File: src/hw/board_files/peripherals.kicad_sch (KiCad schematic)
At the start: 35 parts, among them J3 Screw_Terminal_01x03, J4 Molex 104031-0811, Q1 PMOS, U4 NEO-M9N, U5 BQ27411DRZT-G1A, U6 SHT30-DIS

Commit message: Layout progress
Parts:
- removed JP1, JP2: Solder_Jumper, Jumper:SolderJumper-2_P1.3mm_Open_TrianglePad1.0x1.5mm, symbol Jumper:Jumper_2_Small_Bridged
- TP8, TP9: footprint TestPoint:TestPoint_Pad_D1.5mm -> TestPoint:TestPoint_Pad_D1.0mm
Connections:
- net +3V3: now also U4.1 (~{SAFEBOOT}), U4.2 (D_SEL)
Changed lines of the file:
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@@
 	(wire
 		(pts
-			(xy 40.64 86.36) (xy 53.34 86.36)
+			(xy 40.64 86.36) (xy 63.5 86.36)
 		)
 		(stroke
@@
 	(wire
 		(pts
-			(xy 58.42 86.36) (xy 63.5 86.36)
-		)
-		(stroke
-			(width 0)
-			(type default)
-		)
-	)
-	(wire
-		(pts
-			(xy 58.42 91.44) (xy 63.5 91.44)
-		)
-		(stroke
-			(width 0)
-			(type default)
-		)
-	)
-	(wire
-		(pts
 			(xy 27.94 138.43) (xy 26.67 138.43)
 		)
@@
 	(wire
 		(pts
-			(xy 40.64 91.44) (xy 53.34 91.44)
+			(xy 40.64 91.44) (xy 63.5 91.44)
 		)
 		(stroke
@@
 			)
 		)
-		(property "Footprint" "TestPoint:TestPoint_Pad_D1.5mm"
+		(property "Footprint" "TestPoint:TestPoint_Pad_D1.0mm"
 			(at 137.16 147.32 0)
 			(effects
@@
 	)
 	(symbol
-		(lib_id "Jumper:Jumper_2_Small_Bridged")
-		(at 55.88 91.44 0)
-		(unit 1)
-		(exclude_from_sim no)
-		(in_bom yes)
-		(on_board yes)
-		(dnp no)
-		(fields_autoplaced yes)
-		(property "Reference" "JP2"
-			(at 55.88 93.98 0)
-			(effects
-				(font
-					(size 1.27 1.27)
-				)
-			)
-		)
-		(property "Value" "Solder_Jumper"
-			(at 55.88 96.52 0)
-			(effects
-				(font
-					(size 1.27 1.27)
-				)
-			)
-		)
-		(property "Footprint" "Jumper:SolderJumper-2_P1.3mm_Open_TrianglePad1.0x1.5mm"
-			(at 55.88 91.44 0)
-			(effects
-				(font
-					(size 1.27 1.27)
-				)
-				(hide yes)
-			)
-		)
-		(property "Datasheet" "~"
-			(at 55.88 91.44 0)
-			(effects
-				(font
-					(size 1.27 1.27)
-				)
-				(hide yes)
-			)
-		)
-		(property "Description" "Jumper, 2-pole, small symbol, bridged"
-			(at 55.88 91.44 0)
-			(effects
-				(font
-					(size 1.27 1.27)
-				)
-				(hide yes)
-			)
-		)
-		(pin "1"
-		)
-		(pin "2"
-		)
-		(instances
-			(project ""
-				(path "/2c77a8ba-b277-4959-adec-d3fc778c7960/81382524-b053-4c3c-9e13-c8b314c52639"
-					(reference "JP2")
-					(unit 1)
-				)
-			)
-		)
-	)
-	(symbol
 		(lib_id "Device:R_Small_US")
 		(at 144.78 147.32 270)
@@
 		(on_board yes)
 		(dnp no)
-		(fields_autoplaced yes)
 		(property "Reference" "C22"
 			(at 158.75 151.1235 0)
@@
 					(size 1.27 1.27)
 				)
-				(justify right)
+				(justify left)
 			)
 		)
@@
 	)
 	(symbol
-		(lib_id "Jumper:Jumper_2_Small_Bridged")
-		(at 55.88 86.36 0)
-		(unit 1)
-		(exclude_from_sim no)
-		(in_bom yes)
-		(on_board yes)
-		(dnp no)
-		(property "Reference" "JP1"
-			(at 55.88 81.28 0)
-			(effects
-				(font
-					(size 1.27 1.27)
-				)
-			)
-		)
-		(property "Value" "Solder_Jumper"
-			(at 55.88 83.82 0)
-			(effects
-				(font
-					(size 1.27 1.27)
-				)
-			)
-		)
-		(property "Footprint" "Jumper:SolderJumper-2_P1.3mm_Open_TrianglePad1.0x1.5mm"
-			(at 55.88 86.36 0)
-			(effects
-				(font
-					(size 1.27 1.27)
-				)
-				(hide yes)
-			)
-		)
-		(property "Datasheet" "~"
-			(at 55.88 86.36 0)
-			(effects
-				(font
-					(size 1.27 1.27)
-				)
-				(hide yes)
-			)
-		)
-		(property "Description" "Jumper, 2-pole, small symbol, bridged"
-			(at 55.88 86.36 0)
-			(effects
-				(font
-					(size 1.27 1.27)
-				)
-				(hide yes)
-			)
-		)
-		(pin "1"
-		)
-		(pin "2"
-		)
-		(instances
-			(project "pocket-caddy"
-				(path "/2c77a8ba-b277-4959-adec-d3fc778c7960/81382524-b053-4c3c-9e13-c8b314c52639"
-					(reference "JP1")
-					(unit 1)
-				)
-			)
-		)
-	)
-	(symbol
 		(lib_id "Device:R_Small_US")
 		(at 134.62 152.4 180)
@@
 			)
 		)
-		(property "Footprint" "TestPoint:TestPoint_Pad_D1.5mm"
+		(property "Footprint" "TestPoint:TestPoint_Pad_D1.0mm"
 			(at 250.19 44.45 0)
 			(effects

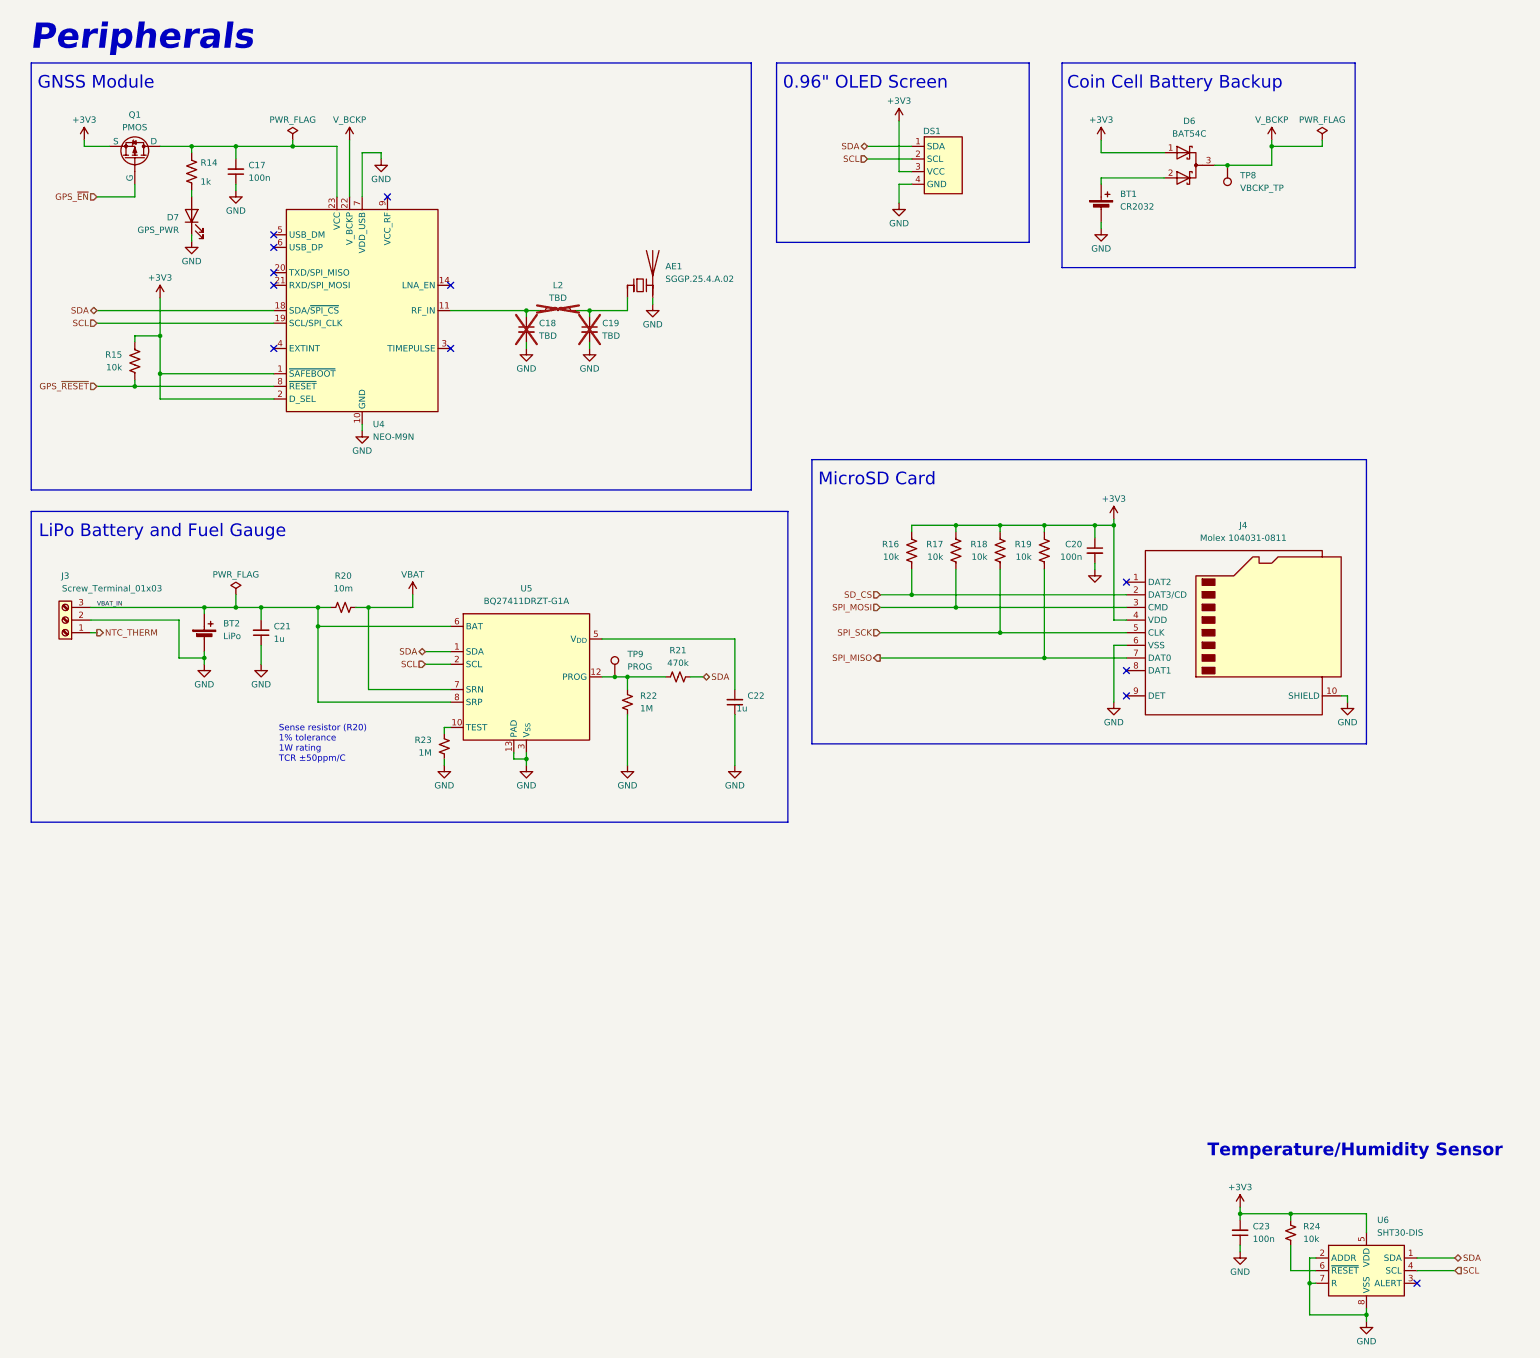
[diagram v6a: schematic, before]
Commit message: New layout done, need to make gerbers
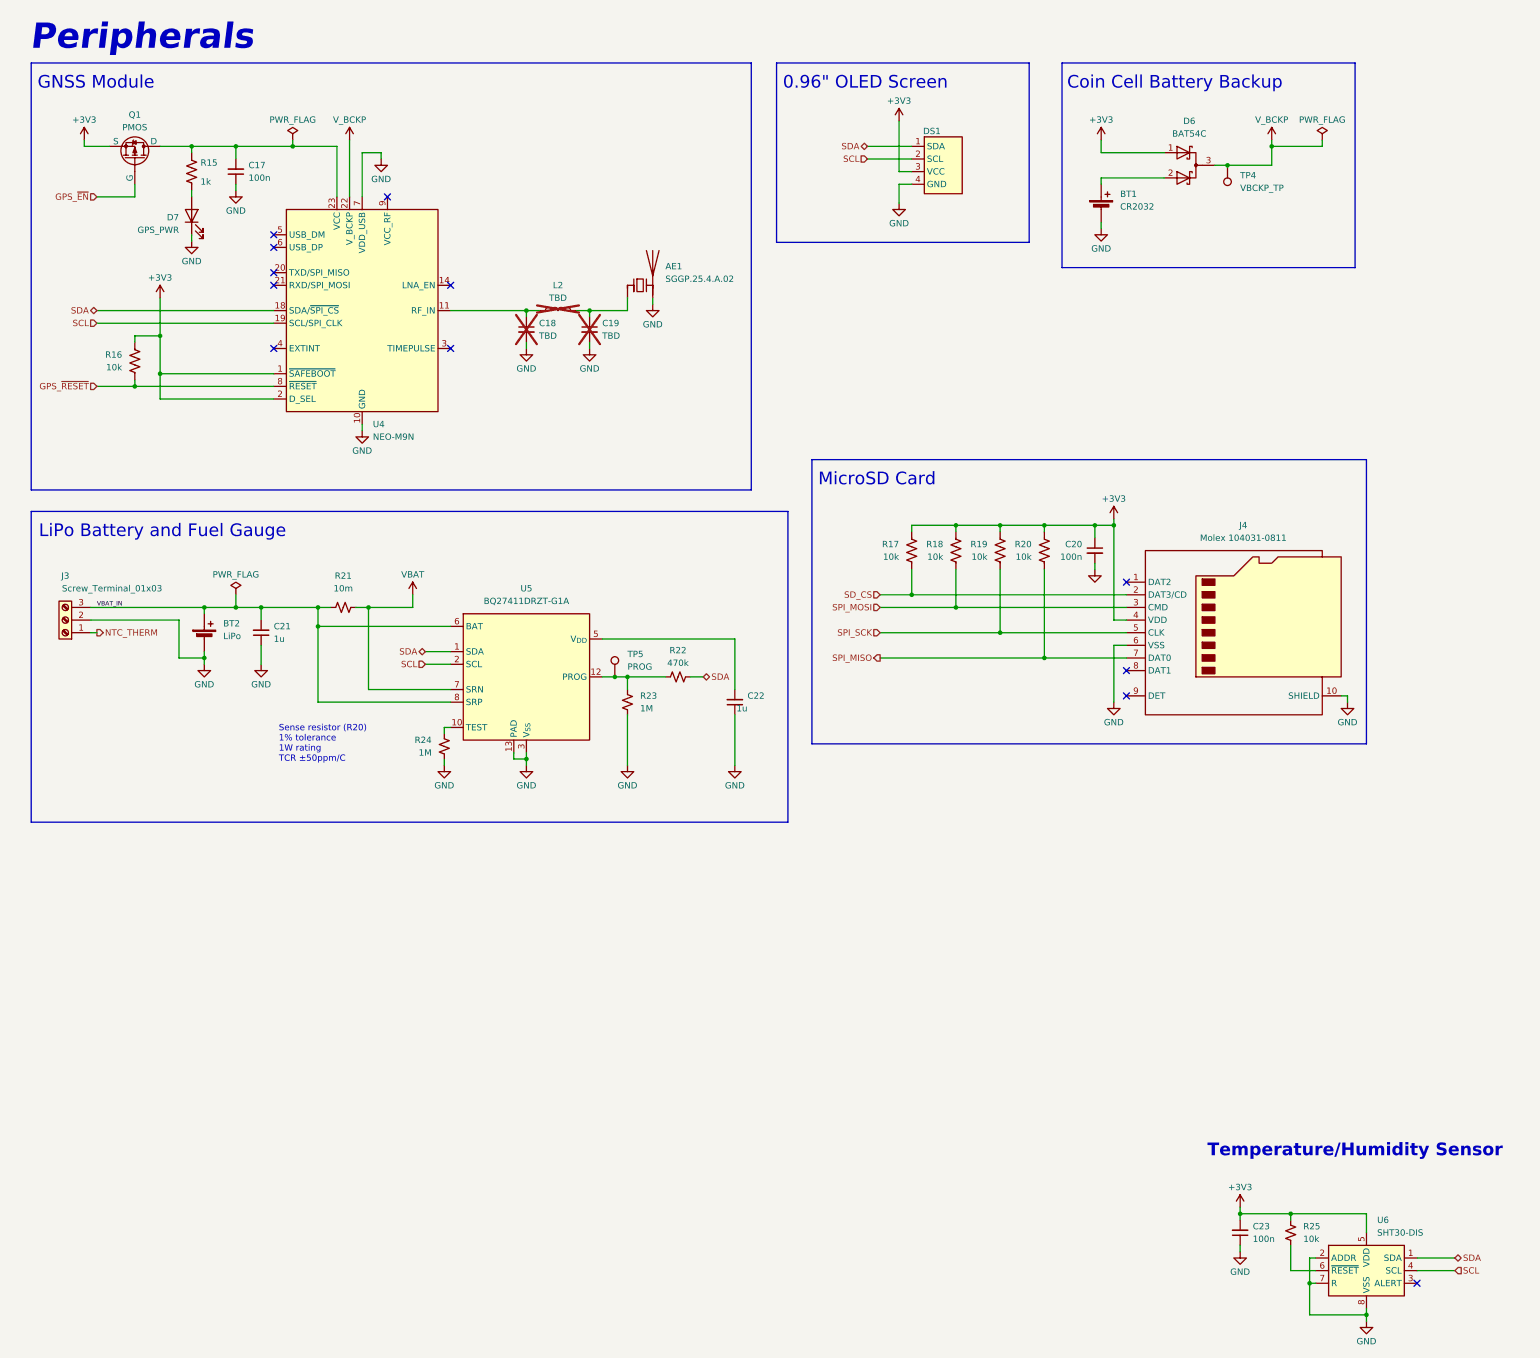
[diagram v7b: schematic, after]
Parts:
- renumbered R14 to R15, R15 to R16, R16 to R17, R17 to R18, R18 to R19, R19 to R20, R20 to R21, R21 to R22, R22 to R23, R23 to R24, R24 to R25, TP8 to TP4, TP9 to TP5

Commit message: rev0.1 done
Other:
- note added: "Sense resistor (R21) 1% tolerance 1W rating TCR ±50ppm/C"
- note removed: "Sense resistor (R20) 1% tolerance 1W rating TCR ±50ppm/C"
- moved on the sheet: C23, R25, U6
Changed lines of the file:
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@@
 		)
 	)
-	(text "Sense resistor (R20)\n1% tolerance\n1W rating\nTCR ±50ppm/C"
+	(text "Sense resistor (R21)\n1% tolerance\n1W rating\nTCR ±50ppm/C"
 		(exclude_from_sim no)
 		(at 64.516 160.782 0)
@@
 	(text "Temperature/Humidity Sensor"
 		(exclude_from_sim no)
-		(at 280.924 242.57 0)
+		(at 193.294 63.5 0)
 		(effects
 			(font
@@
 	)
 	(junction
-		(at 283.21 275.59)
+		(at 195.58 96.52)
 		(diameter 0)
 		(color 0 0 0 0)
@@
 	)
 	(junction
-		(at 271.78 269.24)
+		(at 184.15 90.17)
 		(diameter 0)
 		(color 0 0 0 0)
@@
 	)
 	(junction
-		(at 257.81 255.27)
+		(at 170.18 76.2)
 		(diameter 0)
 		(color 0 0 0 0)
@@
 	)
 	(junction
-		(at 267.97 255.27)
+		(at 180.34 76.2)
 		(diameter 0)
 		(color 0 0 0 0)
@@
 	)
 	(no_connect
-		(at 293.37 269.24)
+		(at 205.74 90.17)
 	)
 	(no_connect
@@
 	(wire
 		(pts
-			(xy 271.78 264.16) (xy 271.78 269.24)
+			(xy 184.15 85.09) (xy 184.15 90.17)
 		)
 		(stroke
@@
 	(wire
 		(pts
-			(xy 271.78 275.59) (xy 283.21 275.59)
+			(xy 184.15 96.52) (xy 195.58 96.52)
 		)
 		(stroke
@@
 	(wire
 		(pts
-			(xy 283.21 274.32) (xy 283.21 275.59)
+			(xy 195.58 95.25) (xy 195.58 96.52)
 		)
 		(stroke
@@
 	(wire
 		(pts
-			(xy 293.37 266.7) (xy 300.99 266.7)
+			(xy 205.74 87.63) (xy 213.36 87.63)
 		)
 		(stroke
@@
 	(wire
 		(pts
-			(xy 257.81 262.89) (xy 257.81 261.62)
+			(xy 170.18 83.82) (xy 170.18 82.55)
 		)
 		(stroke
@@
 	(wire
 		(pts
-			(xy 257.81 254) (xy 257.81 255.27)
+			(xy 170.18 74.93) (xy 170.18 76.2)
 		)
 		(stroke
@@
 	(wire
 		(pts
-			(xy 283.21 275.59) (xy 283.21 276.86)
+			(xy 195.58 96.52) (xy 195.58 97.79)
 		)
 		(stroke
@@
 	(wire
 		(pts
-			(xy 273.05 266.7) (xy 267.97 266.7)
+			(xy 185.42 87.63) (xy 180.34 87.63)
 		)
 		(stroke
@@
 	(wire
 		(pts
-			(xy 267.97 261.62) (xy 267.97 266.7)
+			(xy 180.34 82.55) (xy 180.34 87.63)
 		)
 		(stroke
@@
 	(wire
 		(pts
-			(xy 293.37 264.16) (xy 300.99 264.16)
+			(xy 205.74 85.09) (xy 213.36 85.09)
 		)
 		(stroke
@@
 	(wire
 		(pts
-			(xy 283.21 259.08) (xy 283.21 255.27)
+			(xy 195.58 80.01) (xy 195.58 76.2)
 		)
 		(stroke
@@
 	(wire
 		(pts
-			(xy 273.05 269.24) (xy 271.78 269.24)
+			(xy 185.42 90.17) (xy 184.15 90.17)
 		)
 		(stroke
@@
 	(wire
 		(pts
-			(xy 271.78 269.24) (xy 271.78 275.59)
+			(xy 184.15 90.17) (xy 184.15 96.52)
 		)
 		(stroke
@@
 	(wire
 		(pts
-			(xy 257.81 255.27) (xy 267.97 255.27)
+			(xy 170.18 76.2) (xy 180.34 76.2)
 		)
 		(stroke
@@
 	(wire
 		(pts
-			(xy 267.97 255.27) (xy 267.97 256.54)
+			(xy 180.34 76.2) (xy 180.34 77.47)
 		)
 		(stroke
@@
 	(wire
 		(pts
-			(xy 283.21 255.27) (xy 267.97 255.27)
+			(xy 195.58 76.2) (xy 180.34 76.2)
 		)
 		(stroke
@@
 	(wire
 		(pts
-			(xy 273.05 264.16) (xy 271.78 264.16)
+			(xy 185.42 85.09) (xy 184.15 85.09)
 		)
 		(stroke
@@
 	(wire
 		(pts
-			(xy 257.81 256.54) (xy 257.81 255.27)
+			(xy 170.18 77.47) (xy 170.18 76.2)
 		)
 		(stroke
@@
 	(hierarchical_label "SCL"
 		(shape input)
-		(at 300.99 266.7 0)
+		(at 213.36 87.63 0)
 		(effects
 			(font
@@
 	(hierarchical_label "SDA"
 		(shape bidirectional)
-		(at 300.99 264.16 0)
+		(at 213.36 85.09 0)
 		(effects
 			(font
@@
 	(symbol
 		(lib_id "Device:R_Small_US")
-		(at 267.97 259.08 0)
+		(at 180.34 80.01 0)
 		(unit 1)
 		(exclude_from_sim no)
@@
 		(fields_autoplaced yes)
 		(property "Reference" "R25"
-			(at 270.51 257.8099 0)
+			(at 182.88 78.7399 0)
 			(effects
 				(font
@@
 		)
 		(property "Value" "10k"
-			(at 270.51 260.3499 0)
+			(at 182.88 81.2799 0)
 			(effects
 				(font
@@
 		)
 		(property "Footprint" "Resistor_SMD:R_0603_1608Metric_Pad0.98x0.95mm_HandSolder"
-			(at 267.97 259.08 0)
+			(at 180.34 80.01 0)
 			(effects
 				(font
@@
 		)
 		(property "Datasheet" "~"
-			(at 267.97 259.08 0)
+			(at 180.34 80.01 0)
 			(effects
 				(font
@@
 		)
 		(property "Description" "Resistor, small US symbol"
-			(at 267.97 259.08 0)
+			(at 180.34 80.01 0)
 			(effects
 				(font
@@
 	(symbol
 		(lib_id "power:GND")
-		(at 257.81 262.89 0)
+		(at 170.18 83.82 0)
 		(unit 1)
 		(exclude_from_sim no)
@@
 		(dnp no)
 		(property "Reference" "#PWR074"
-			(at 257.81 269.24 0)
+			(at 170.18 90.17 0)
 			(effects
 				(font
@@
 		)
 		(property "Value" "GND"
-			(at 257.81 266.954 0)
+			(at 170.18 87.884 0)
 			(effects
 				(font
@@
 		)
 		(property "Footprint" ""
-			(at 257.81 262.89 0)
+			(at 170.18 83.82 0)
 			(effects
 				(font
@@
 		)
 		(property "Datasheet" ""
-			(at 257.81 262.89 0)
+			(at 170.18 83.82 0)
 			(effects
 				(font
@@
 		)
 		(property "Description" "Power symbol creates a global label with name \"GND\" , ground"
-			(at 257.81 262.89 0)
+			(at 170.18 83.82 0)
 			(effects
 				(font
@@
 	(symbol
 		(lib_id "power:GND")
-		(at 283.21 276.86 0)
+		(at 195.58 97.79 0)
 		(unit 1)
 		(exclude_from_sim no)
@@
 		(dnp no)
 		(property "Reference" "#PWR075"
-			(at 283.21 283.21 0)
+			(at 195.58 104.14 0)
 			(effects
 				(font
@@
 		)
 		(property "Value" "GND"
-			(at 283.21 280.924 0)
+			(at 195.58 101.854 0)
 			(effects
 				(font
@@
 		)
 		(property "Footprint" ""
-			(at 283.21 276.86 0)
+			(at 195.58 97.79 0)
 			(effects
 				(font
@@
 		)
 		(property "Datasheet" ""
-			(at 283.21 276.86 0)
+			(at 195.58 97.79 0)
 			(effects
 				(font
@@
 		)
 		(property "Description" "Power symbol creates a global label with name \"GND\" , ground"
-			(at 283.21 276.86 0)
+			(at 195.58 97.79 0)
 			(effects
 				(font
@@
 		(on_board yes)
 		(dnp no)
+		(fields_autoplaced yes)
 		(property "Reference" "C22"
 			(at 158.75 151.1235 0)
@@
 					(size 1.27 1.27)
 				)
-				(justify left)
+				(justify right)
 			)
 		)
@@
 	(symbol
 		(lib_id "Sensor_Humidity:SHT30-DIS")
-		(at 283.21 266.7 0)
+		(at 195.58 87.63 0)
 		(unit 1)
 		(exclude_from_sim no)
@@
 		(fields_autoplaced yes)
 		(property "Reference" "U6"
-			(at 285.3533 256.54 0)
+			(at 197.7233 77.47 0)
 			(effects
 				(font
@@
 		)
 		(property "Value" "SHT30-DIS"
-			(at 285.3533 259.08 0)
+			(at 197.7233 80.01 0)
 			(effects
 				(font
@@
 		)
 		(property "Footprint" "Sensor_Humidity:Sensirion_DFN-8-1EP_2.5x2.5mm_P0.5mm_EP1.1x1.7mm"
-			(at 283.21 265.43 0)
+			(at 195.58 86.36 0)
 			(effects
 				(font
@@
 		)
 		(property "Datasheet" "https://sensirion.com/media/documents/213E6A3B/63A5A569/Datasheet_SHT3x_DIS.pdf"
-			(at 283.21 265.43 0)
+			(at 195.58 86.36 0)
 			(effects
 				(font
@@
 		)
 		(property "Description" "I²C humidity and temperature sensor, ±2%RH, ±0.2°C, DFN-8"
-			(at 283.21 266.7 0)
+			(at 195.58 87.63 0)
 			(effects
 				(font
@@
 	(symbol
 		(lib_id "Device:C_Small")
-		(at 257.81 259.08 180)
+		(at 170.18 80.01 180)
 		(unit 1)
 		(exclude_from_sim no)
@@
 		(fields_autoplaced yes)
 		(property "Reference" "C23"
-			(at 260.35 257.8035 0)
+			(at 172.72 78.7335 0)
 			(effects
 				(font
@@
 		)
 		(property "Value" "100n"
-			(at 260.35 260.3435 0)
+			(at 172.72 81.2735 0)
 			(effects
 				(font
@@
 		)
 		(property "Footprint" "Capacitor_SMD:C_0603_1608Metric_Pad1.08x0.95mm_HandSolder"
-			(at 257.81 259.08 0)
+			(at 170.18 80.01 0)
 			(effects
 				(font
@@
 		)
 		(property "Datasheet" "~"
-			(at 257.81 259.08 0)
+			(at 170.18 80.01 0)
 			(effects
 				(font
@@
 		)
 		(property "Description" "Unpolarized capacitor, small symbol"
-			(at 257.81 259.08 0)
+			(at 170.18 80.01 0)
 			(effects
 				(font
@@
 	(symbol
 		(lib_id "power:+3V3")
-		(at 257.81 254 0)
+		(at 170.18 74.93 0)
 		(unit 1)
 		(exclude_from_sim no)
@@
 		(dnp no)
 		(property "Reference" "#PWR073"
-			(at 257.81 257.81 0)
+			(at 170.18 78.74 0)
 			(effects
 				(font
@@
 		)
 		(property "Value" "+3V3"
-			(at 257.81 249.936 0)
+			(at 170.18 70.866 0)
 			(effects
 				(font
@@
 		)
 		(property "Footprint" ""
-			(at 257.81 254 0)
+			(at 170.18 74.93 0)
 			(effects
 				(font
@@
 		)
 		(property "Datasheet" ""
-			(at 257.81 254 0)
+			(at 170.18 74.93 0)
 			(effects
 				(font
@@
 		)
 		(property "Description" "Power symbol creates a global label with name \"+3V3\""
-			(at 257.81 254 0)
+			(at 170.18 74.93 0)
 			(effects
 				(font
